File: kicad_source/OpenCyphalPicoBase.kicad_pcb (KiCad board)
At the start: 2 copper layers, 52 x 36 mm, 63 parts, among them CN1 RASPBERRYPI_PICO, CN11 DNI, CN12 S3B-PH-SM4-TB, CN2 SM04B-SRSS-TB, CN3 SM04B-SRSS-TB, CN4 SM04B-GHS-TB, CN5 SM04B-GHS-TB, CN6 691322310002, CN7 DNI, CN8 DNI, SW1 PTS636 SM43 SMTR LFS, U3 24LC64-I/SN, U8 MCP2515-I/SO, U9 SN65HVD232, Y1 RH100-16.000-16-3030-EXT-TR

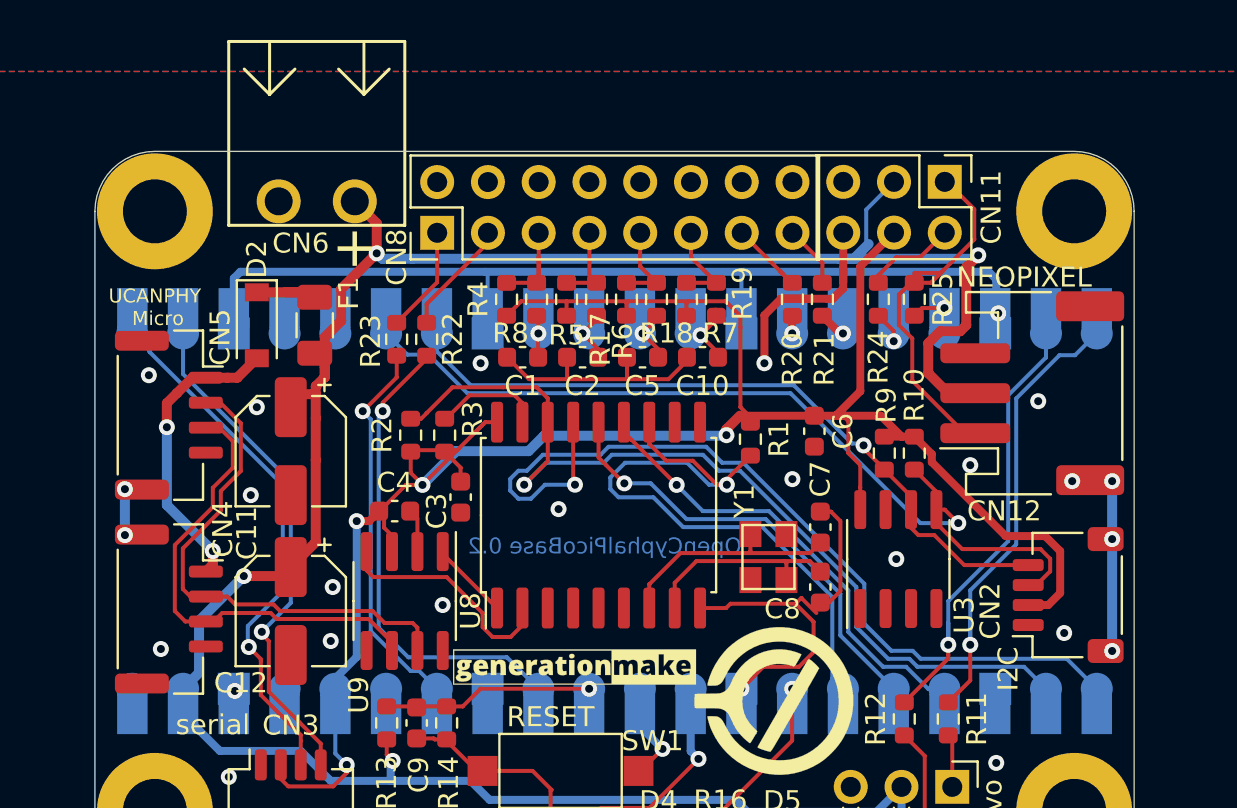
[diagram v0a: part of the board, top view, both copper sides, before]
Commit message: combined CN6, CN8 and CN11 into one connector
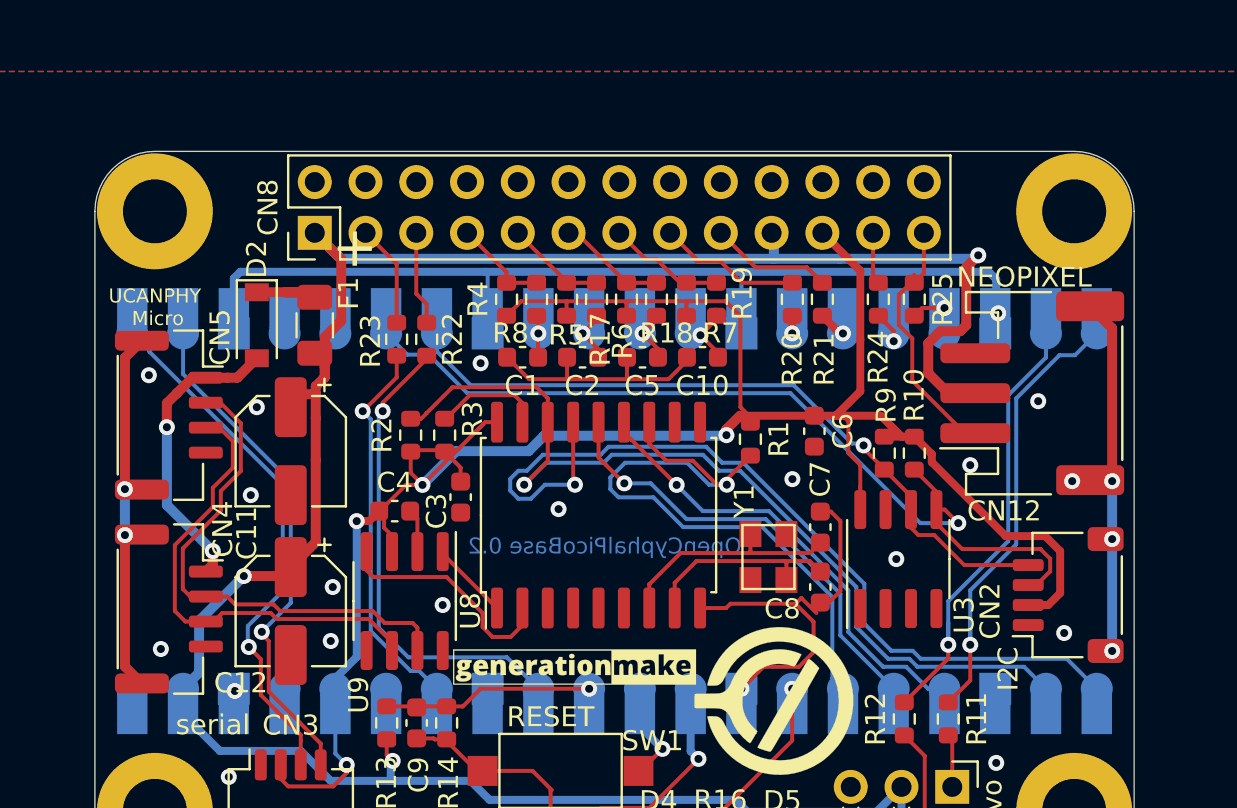
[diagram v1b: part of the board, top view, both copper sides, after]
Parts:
- removed CN11: DNI, Connector_PinHeader_2.54mm:PinHeader_2x03_P2.54mm_Vertical
- removed CN6: 691322310002, CON_wuerth:WR-TBL_691322310002
- CN8: footprint Connector_PinHeader_2.54mm:PinHeader_2x08_P2.54mm_Vertical -> Connector_PinHeader_2.54mm:PinHeader_2x13_P2.54mm_Vertical
- D4: value 150060YS75000 -> NCD0603Y1
- D5: value 150060RS75000 -> KT-0603R
- F1: value nanoSMDC050F -> nSMD050-33V
- U3: value 24LC64-I/SN -> M24C64-RMN6TP
- U8: value MCP2515-I/SO -> MCP2515T-I/SO
- U9: value SN65HVD232 -> SN65HVD230
- Y1: value RH100-16.000-16-3030-EXT-TR -> X322516MLB4SI
- moved CN8 6.12 mm to (75.0, 78.1)
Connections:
- CN8 pad 1: /ANALOG_INPUT1_R -> +BATT
- CN8 pad 11: /INPUT3_R -> /INPUT2_R
- CN8 pad 13: /OUTPUT0_R -> /INPUT3_R
- CN8 pad 15: /OUTPUT1_R -> /OUTPUT0_R
- CN8 pad 3: /ANALOG_INPUT0_R -> /ANALOG_INPUT1_R
- CN8 pad 5: /INPUT0_R -> /ANALOG_INPUT0_R
- CN8 pad 7: /INPUT1_R -> /INPUT0_R
- CN8 pad 9: /INPUT2_R -> /INPUT1_R
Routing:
- net /MCP2515/MP1: track 2.30 -> 17.9 mm
- net GND: track 118.0 -> 105.4 mm, vias 20 -> 19
- net /MP2: track 10.5 -> 19.7 mm
- net /NEOPIXEL_R: track 19.1 -> 12.8 mm
- net /OUTPUT0_R: track 3.81 -> 7.25 mm
- net +BATT: track 123.7 -> 120.7 mm, vias 4 -> 3
- net /OUTPUT1_R: track 3.12 -> 6.12 mm
- net /RESERVED0_R: track 4.58 -> 2.61 mm
- net /INPUT3_R: track 4.53 -> 5.90 mm
- net /INPUT2_R: track 4.34 -> 5.44 mm
- net /ANALOG_INPUT0_R: track 5.77 -> 4.72 mm
- net /INPUT1_R: track 4.15 -> 5.01 mm

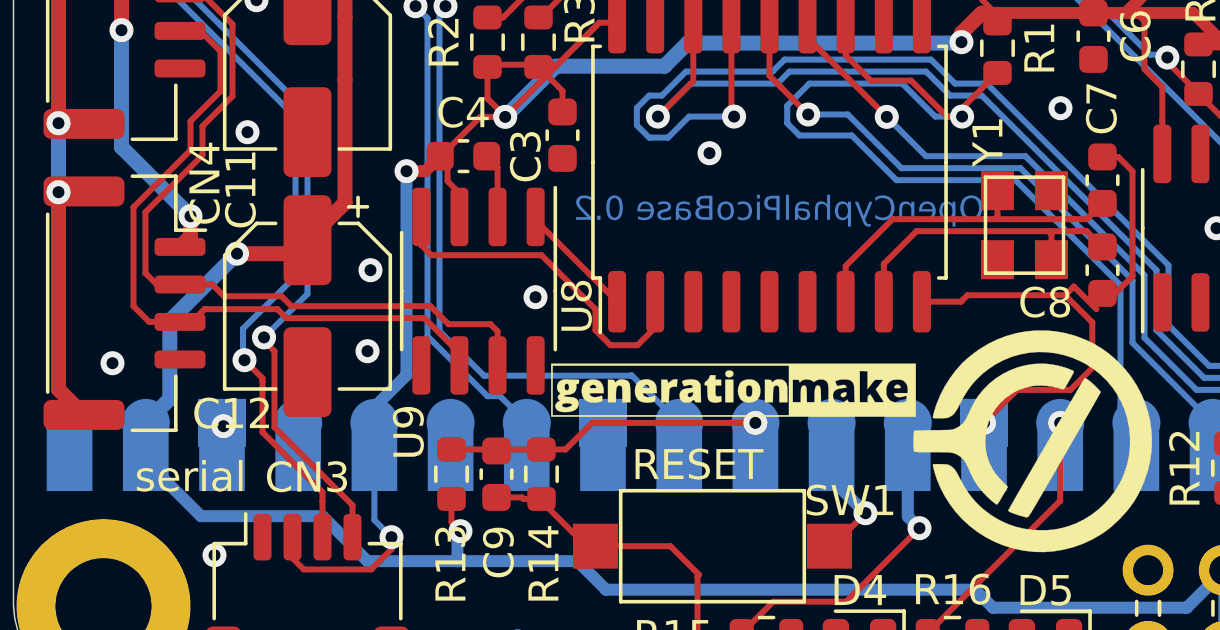
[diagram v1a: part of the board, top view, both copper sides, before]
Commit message: removed C12, added CAN protection, updated schematic
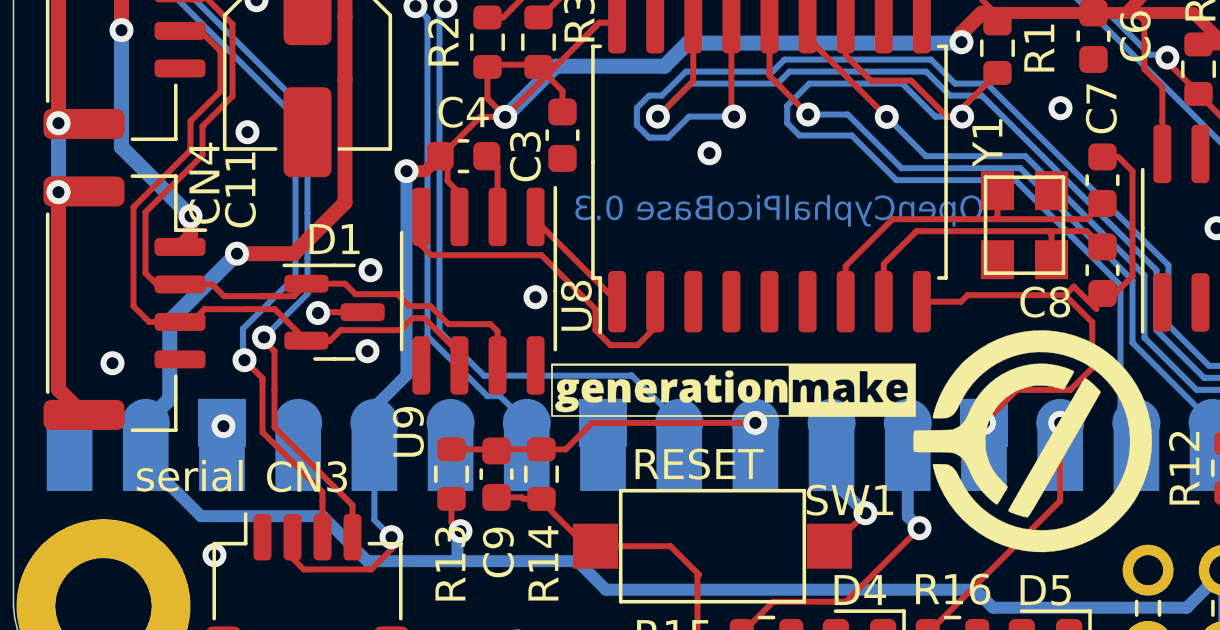
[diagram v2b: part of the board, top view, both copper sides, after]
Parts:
- removed C12: 100 uF / 6,3 V, Capacitor_SMD:CP_Elec_5x5.3
- added D1: NUP2105L, Package_TO_SOT_SMD:SOT-23, F.Cu at (74.7, 97.2)
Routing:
- net GND: track 105.4 -> 106.9 mm, vias 19 -> 20
- net /MCP2515/CANH: track 25.4 -> 26.4 mm
- net /MCP2515/CANL: track 23.8 -> 24.4 mm
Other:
- board text added: "+3V3"
- board text added: "OpenCyphalPicoBase 0.3"
- board text added: "V_IN"
- board text removed: "OpenCyphalPicoBase 0.2"
- board text removed: "V_IN | GND"

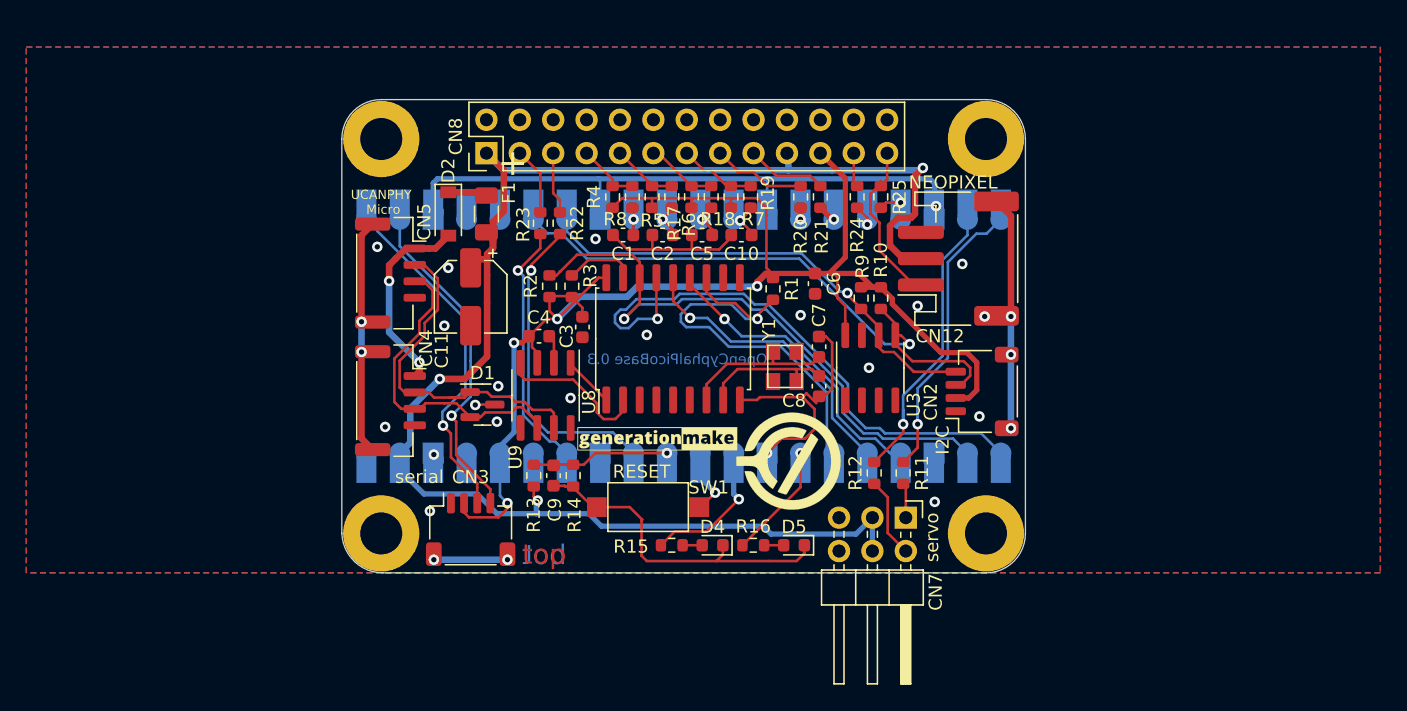
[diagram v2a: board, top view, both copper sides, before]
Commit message: added qwiic logo, made DRC
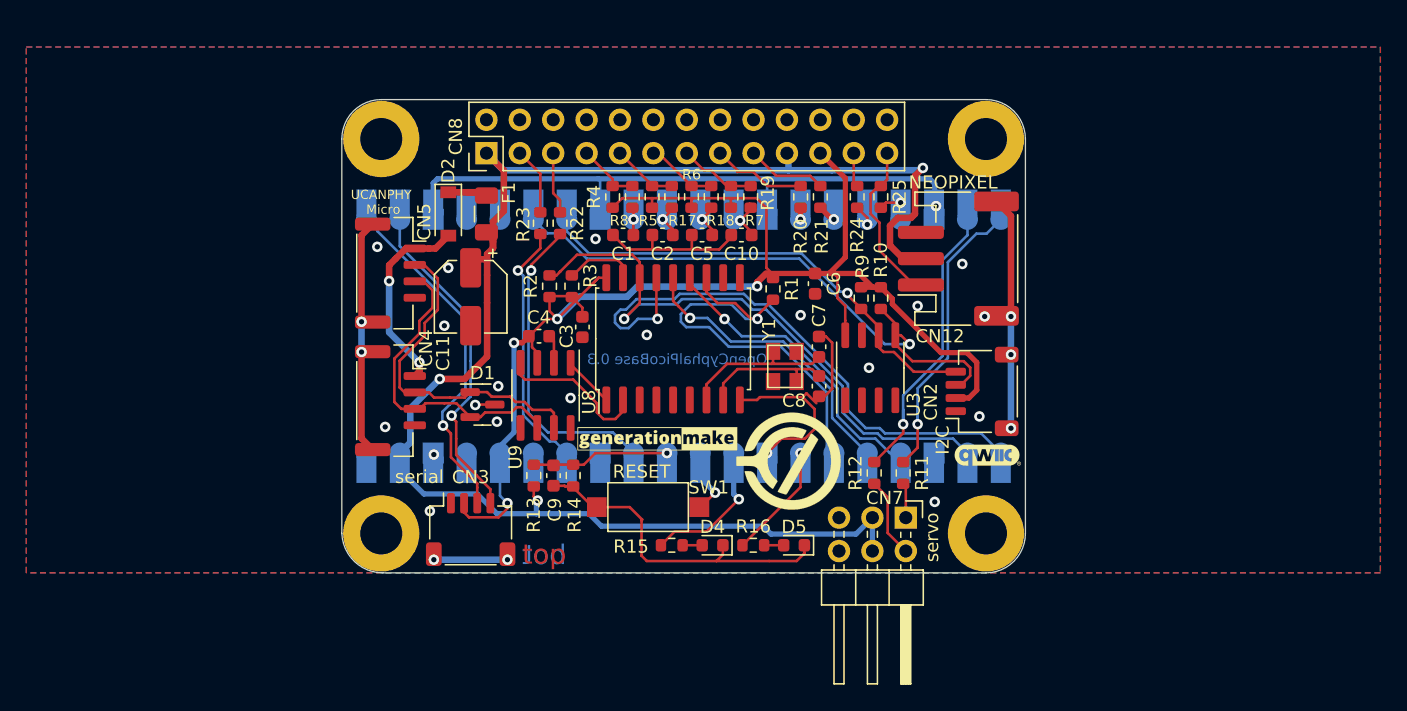
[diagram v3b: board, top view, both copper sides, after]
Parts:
- added L4: Label, generationmake:qwiic_logo, F.Cu at (113.1, 101.0)
- D1: value NUP2105L -> DNI
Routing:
- net /MCP2515/CANH: track 26.4 -> 25.7 mm
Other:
- board text added: "T | + | -"
- board text removed: "+"
